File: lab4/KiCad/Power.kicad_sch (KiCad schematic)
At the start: 47 parts, among them J40 BATTERY IN, J41 VBAT test, J42 Rail / PG / GND, J43 Rail / PG / GND, J44 Rail / PG / GND, Q1 DMPH3010LK3-13, U40 TPS564252DRLR, U41 TPS564252DRLR, U42 TPS564252DRLR

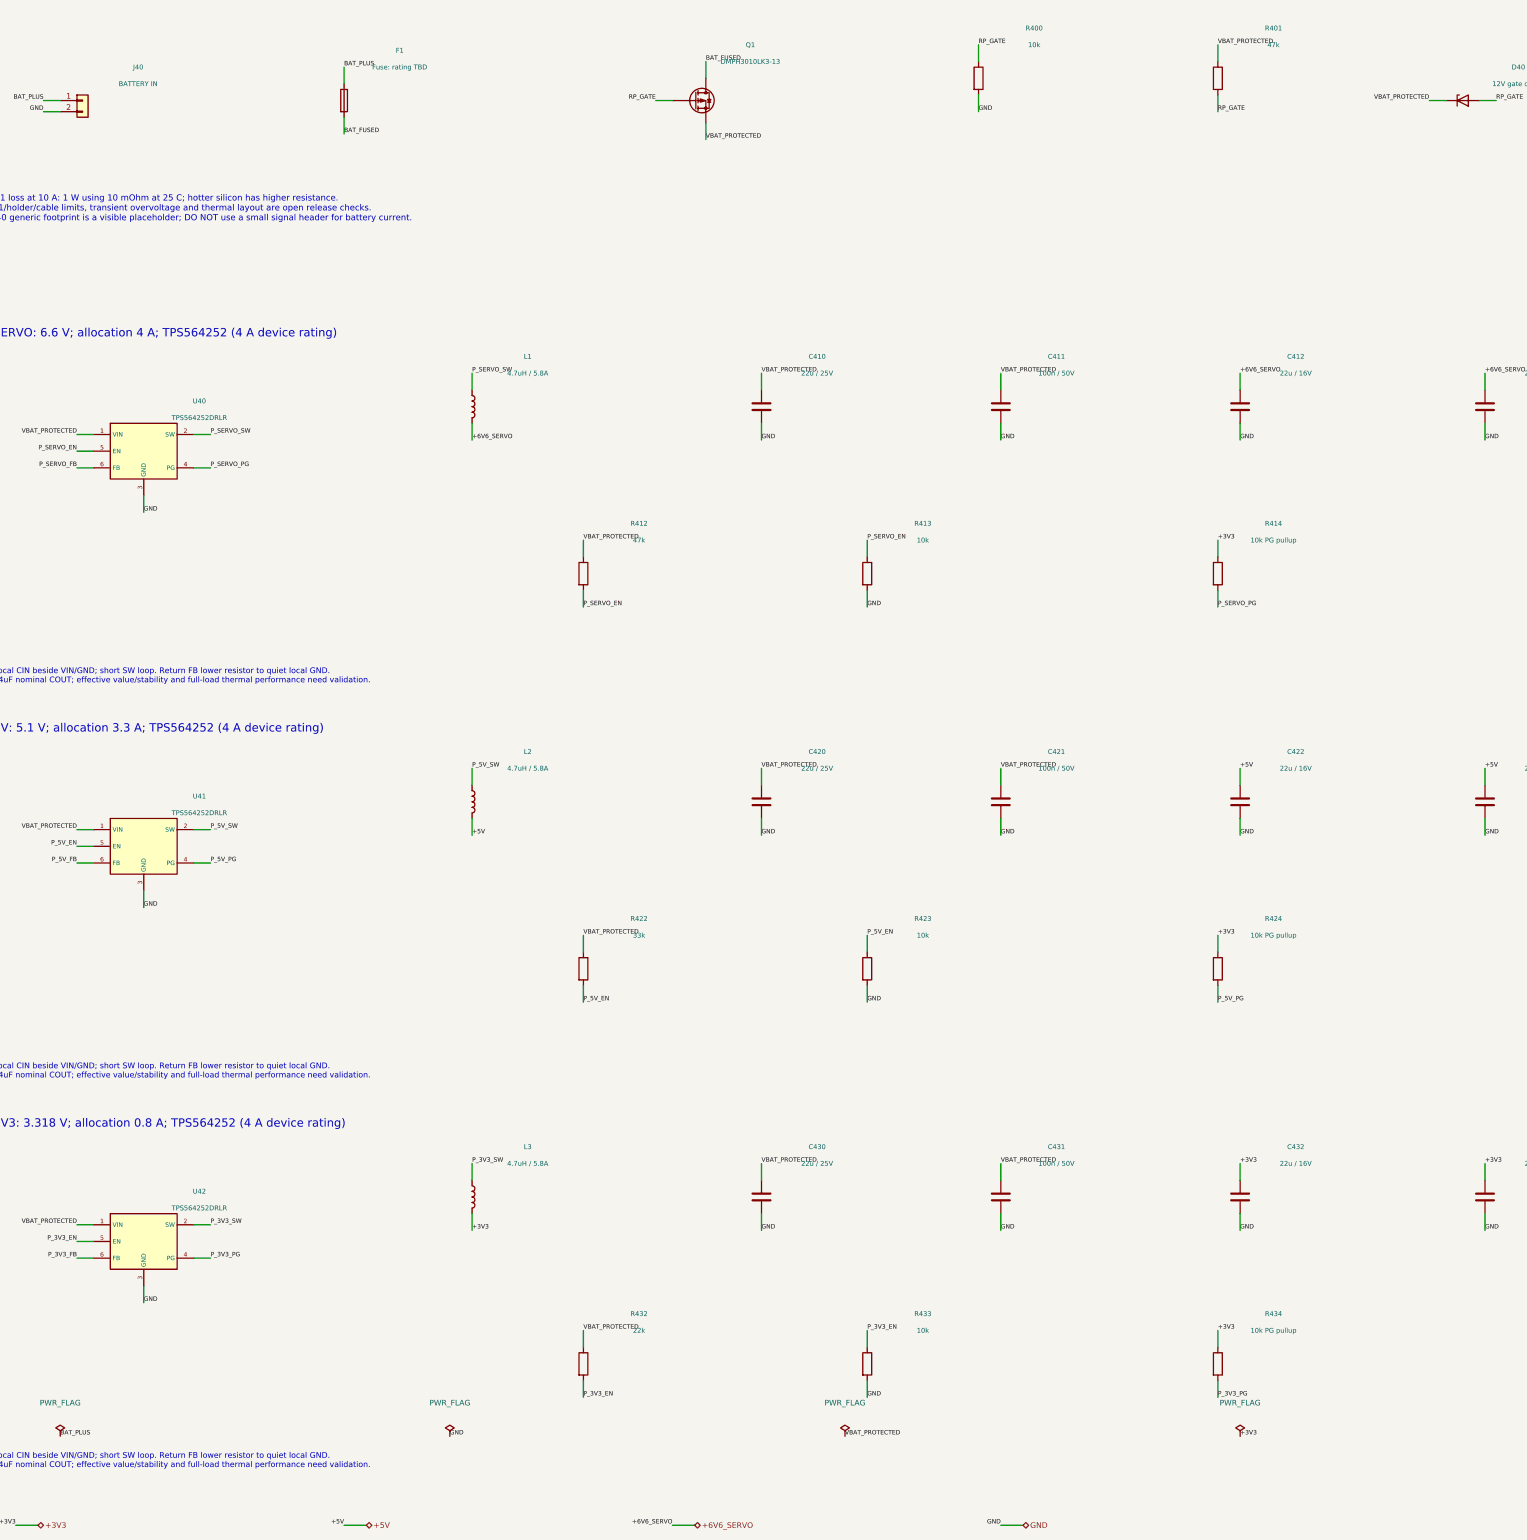
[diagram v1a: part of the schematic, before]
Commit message: Update Lab 4 circuits, assembly BOMs and measured PCB placement
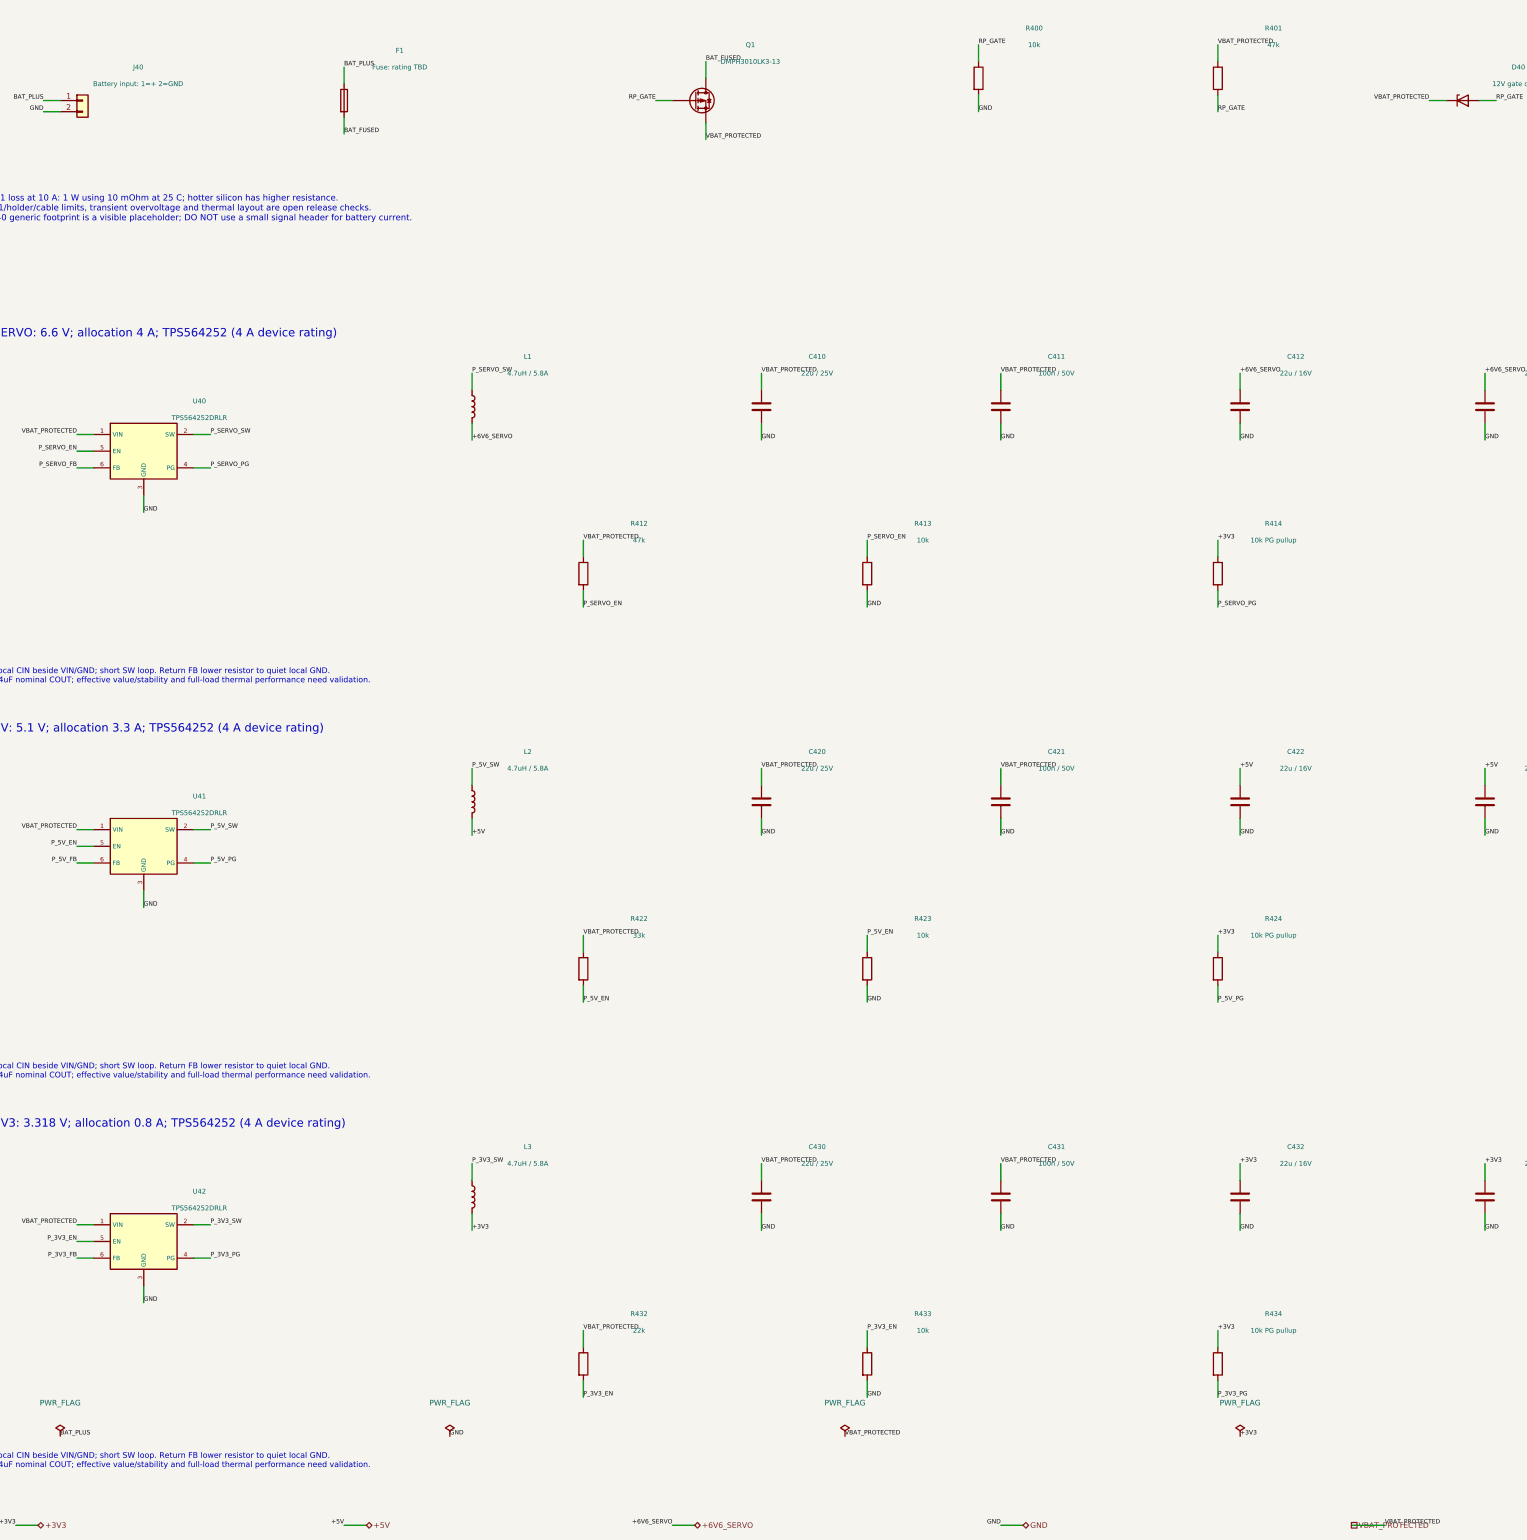
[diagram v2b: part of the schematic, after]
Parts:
- J40: value BATTERY IN -> Battery input: 1=+ 2=GND; footprint Connector_PinHeader_2.54mm:PinHeader_1x02_P2.54mm_Vertical -> Connector_Hirose:Hirose_DF63M-2P-3.96DSA_1x02_P3.96mm_Vertical; Design status Electrical placeholder only: replace generic header footpri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 -> Teammate connector proposal; 14A header rating; verify wire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; MPN FIT0587 -> DF63M-2P-3.96DSA

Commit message: Prepare Lab 4 review package and align course assembly plan
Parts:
- D40: MPN BZT52C12 (Diotec) -> BZT52C12
- F1: MPN 3568 holder; fuse TBD -> 3568
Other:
- note added: "NiMH PACK INPUT - 10 cells; AA or Sub-C pack selection pending"
- note added: "Q1 loss at 10 A: 1 W using 10 mOhm at 25 C; hotter silicon has higher resistance. F1/holder/cable limits, transient overvoltage and thermal layout are open release checks. J40 is Hirose DF63M-2P-3.96DSA; verify mating contacts, wire gauge, polarity and fuse coordination."
- note removed: "AA PACK INPUT - 10x NiMH recommended; exact cells/holder not selected"
- note removed: "Q1 loss at 10 A: 1 W using 10 mOhm at 25 C; hotter silicon has higher resistance. F1/holder/cable limits, transient overvoltage and thermal layout are open release checks. J40 generic footprint is a visible placeholder; DO NOT use a small signal header for battery current."
- title: Power - AA input and three buck converters -> Power - NiMH input and three buck converters

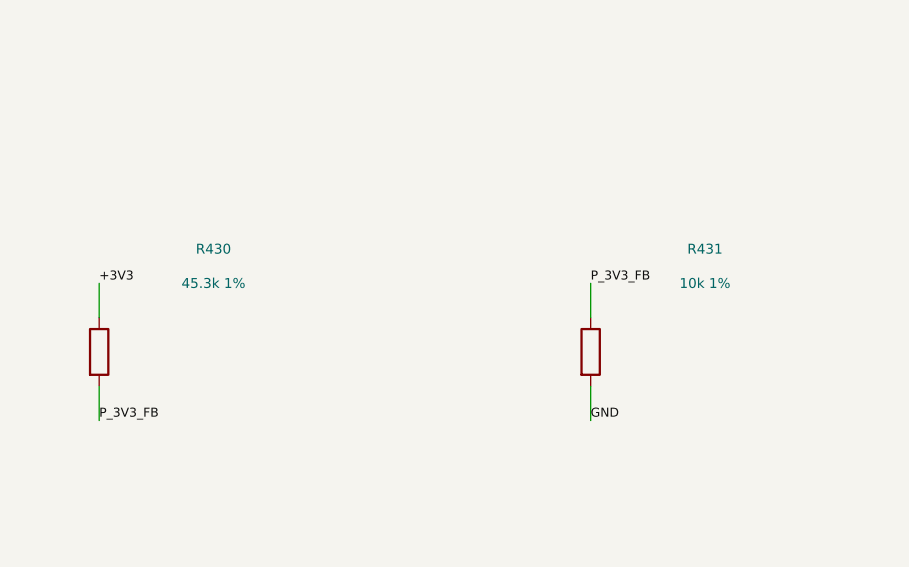
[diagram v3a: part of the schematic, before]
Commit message: Review supply margins, CAN topology and fabrication clearances
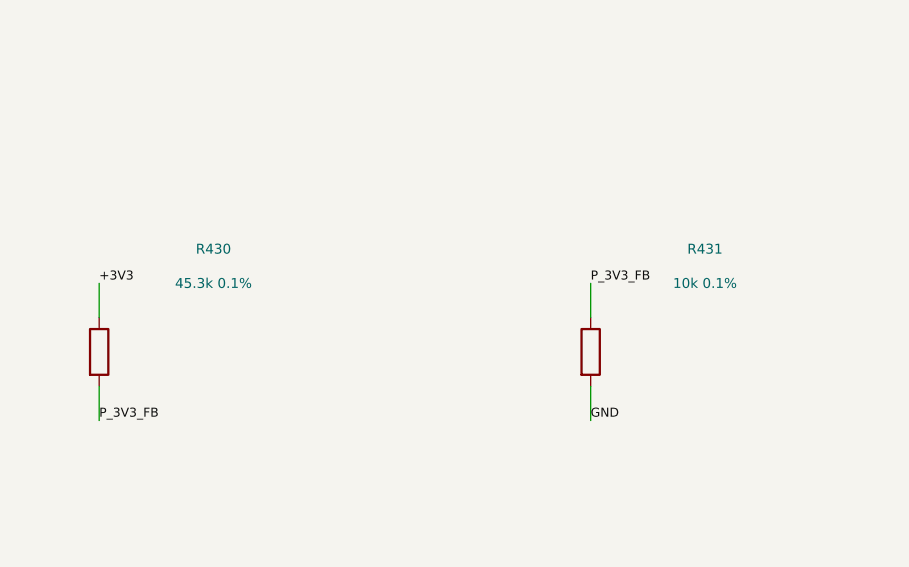
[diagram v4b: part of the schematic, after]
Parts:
- R430: value 45.3k 1% -> 45.3k 0.1%; MPN RC0603FR-0745K3L -> RT0603BRD0745K3L
- R431: value 10k 1% -> 10k 0.1%; MPN CRCW060310K0FKEA -> RT0603BRD0710KL

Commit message: Add chassis mounting allowance and revise power capacitor banks
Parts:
- added C415, C416, C417, C418, C425, C426, C427, C435, C436, C437: 22u 25V, Capacitor_SMD:C_1210_3225Metric, symbol Device:C
- C412, C413, C422, C423, C432, C433: value 22u / 16V -> 22u 25V; footprint Capacitor_SMD:C_0805_2012Metric -> Capacitor_SMD:C_1210_3225Metric; Design status Check effective capacitance under DC bias -> 22uF 25V X5R +/-10%; parallel bank accounts for DC-bias los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; MPN GRM219R61C226ME15L -> GRM32ER61E226KE15L
- C414: value 22p C0G -> 68p C0G; Design status Feed-forward value is a starting point within TI 10-100 pF 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 -> Revised with capacitor banks: servo/Pi zero near 23kHz; log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; MPN C0603C220J1GACTU -> GRM1885C1H680JA01D
- C424: value 22p C0G -> 91p C0G; Design status Feed-forward value is a starting point within TI 10-100 pF 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 -> Revised with capacitor banks: servo/Pi zero near 23kHz; log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; MPN C0603C220J1GACTU -> GRM1885C1H910JA01D
- C434: value 22p C0G -> 30p C0G; Design status Feed-forward value is a starting point within TI 10-100 pF 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 -> Revised with capacitor banks: servo/Pi zero near 23kHz; log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; MPN C0603C220J1GACTU -> GRM1885C1H300JA01D
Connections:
- net +3V3: now also C437.1
- net +5V: now also C427.1
- net +6V6_SERVO: now also C417.1, C418.1
- net GND: now also C415.2, C416.2, C417.2, C418.2, C425.2, C426.2, C427.2, C435.2, C436.2, C437.2
- net VBAT_PROTECTED: now also C415.1, C416.1, C425.1, C426.1, C435.1, C436.1
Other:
- note added: "3 x 22uF CIN + 100nF; 3 x 22uF COUT, GRM32ER61E226KE15L (25V/1210). DC-bias/tolerance/temperature/aging sensitivities documented; loop/transient/thermal behavior unmeasured."
- note added: "3 x 22uF CIN + 100nF; 4 x 22uF COUT, GRM32ER61E226KE15L (25V/1210). DC-bias/tolerance/temperature/aging sensitivities documented; loop/transient/thermal behavior unmeasured."
- note added: "3S LiPo INPUT - CNHL S220403BK / XT60; external Hitec 44295 balance charger"
- note added: "Selected pack: 11.1 V nominal / 12.6 V full. Circuit review envelope: 8-15 V. Battery/motor rail is UNREGULATED. Pack /11 monitor on Front PA3; firmware cutoff must be integrated. Disconnect and balance-charge off the car. No onboard lithium charger, BMS or hard undervoltage disconnect."
- note removed: "Design input envelope: 8-15 V at the protected node; verify real cells, contact resistance and sag. Battery / motor rail is UNREGULATED. No lithium charger or lithium BMS is included."
- note removed: "Local CIN beside VIN/GND; short SW loop. Return FB lower resistor to quiet local GND. 44uF nominal COUT; effective value/stability and full-load thermal performance need validation."
- note removed: "NiMH PACK INPUT - 10 cells; AA or Sub-C pack selection pending"
- title: Power - NiMH input and three buck converters -> Power - 3S LiPo input and three buck converters
